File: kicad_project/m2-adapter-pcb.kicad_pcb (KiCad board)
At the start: 2 copper layers, 102 x 43 mm, 29 parts, among them J1 SATA-7P, J2 JST S2B-PH-K-S, J3 Bus_M.2_Socket_B, U1 LMR33630ADDA

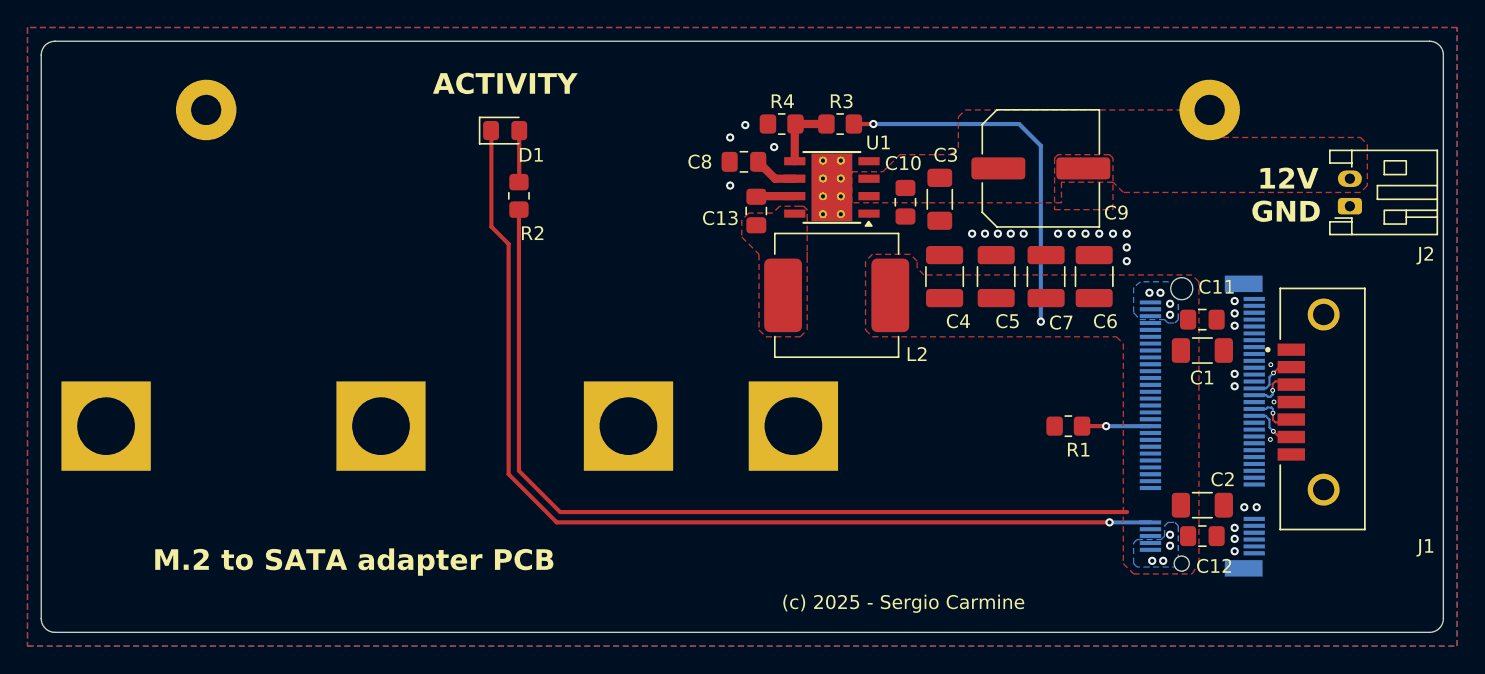
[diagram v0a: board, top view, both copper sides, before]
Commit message: Buck converter redesign
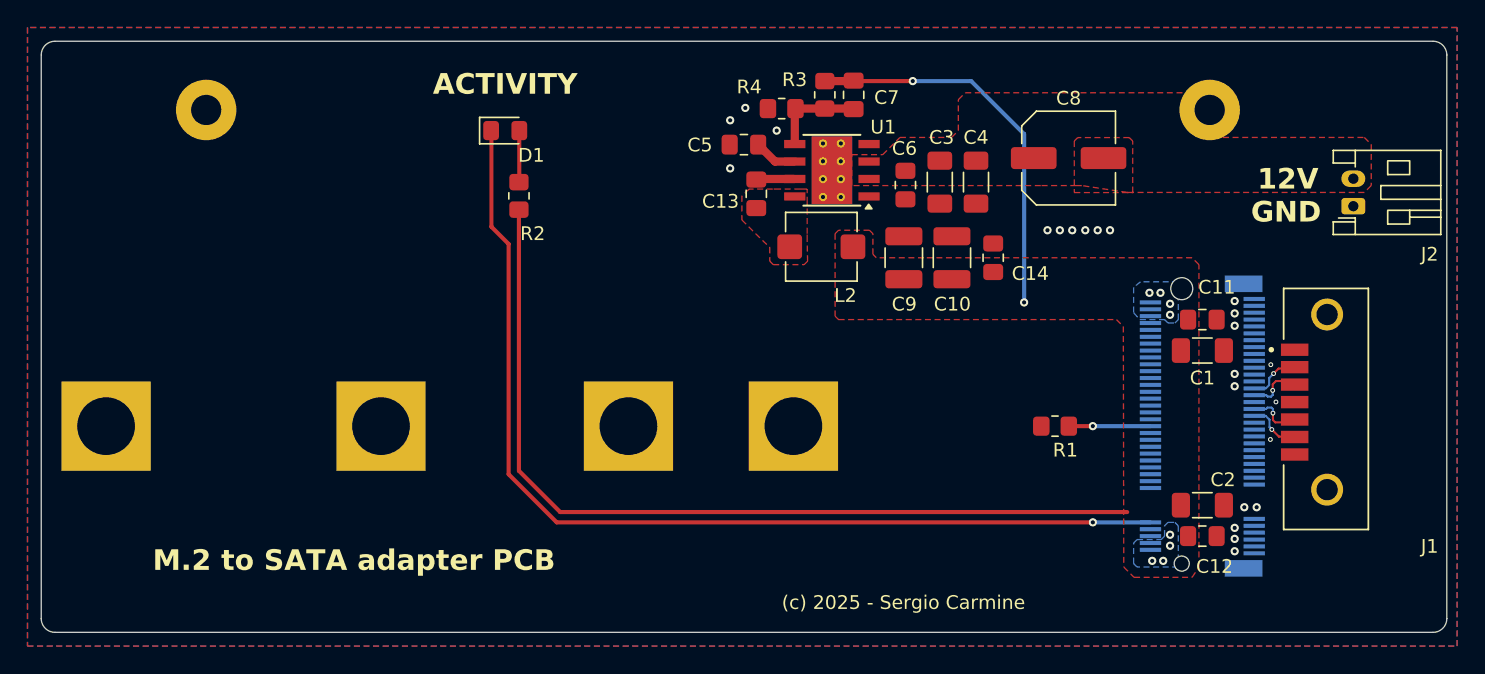
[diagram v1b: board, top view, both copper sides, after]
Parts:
- removed the C5 at (169.1, 64.1)
- removed the C6 at (172.6, 64.1)
- added C14: 0.1uF, Capacitor_SMD:C_0805_2012Metric_Pad1.18x1.45mm_HandSolder, F.Cu at (165.2, 62.8)
- added C4: 10uF, Capacitor_SMD:C_1206_3216Metric_Pad1.33x1.80mm_HandSolder, F.Cu at (164.0, 57.2)
- added C7: 4.7pF, Capacitor_SMD:C_0805_2012Metric_Pad1.18x1.45mm_HandSolder, F.Cu at (155.1, 50.9)
- C8: renamed from C9; value 100uF -> 47uF; footprint Capacitor_SMD:C_Elec_8x6.2 -> Capacitor_SMD:C_Elec_6.3x5.8
- L2: value 6.8uH -> 2.2uH; footprint m2-adapter-pcb:L_MPX1D0840 -> m2-adapter-pcb:L_AMDLA4530S
- U1: value LMR33630ADDA -> LMR33630BDDA; footprint Package_SO:Texas_HSOP-8-1EP_3.9x4.9mm_P1.27mm_ThermalVias -> m2-adapter-pcb:Texas_HSOP-8-1EP_3.9x4.9mm_P1.27mm_ThermalVias_HandSolder
- moved L2 3.71 mm to (152.8, 62.0)
- moved C10 3.50 mm to (162.2, 62.8)
- moved C9 3.27 mm to (158.8, 62.8)
- moved R3 2.40 mm to (153.0, 50.9), turned to 90 degrees
- moved C8 2.15 mm to (170.7, 55.5)
- moved C13 1.25 mm to (148.0, 58.1)
- moved C3 1.25 mm to (161.4, 57.2)
- moved C5 1.25 mm to (147.1, 54.5)
- moved C6 1.25 mm to (158.9, 57.5)
- moved U1 1.25 mm to (153.5, 56.4)
- moved R4 1.12 mm to (149.9, 51.9)
- moved R1 0.97 mm to (169.8, 75.0)
- moved J1 0.25 mm to (189.5, 73.8)
- moved J2 0.25 mm to (191.4, 59.0)
- renumbered C7 to C10, C8 to C5, C10 to C6, C4 to C9
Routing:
- net Net-(U1-FB): track 4.98 -> 7.02 mm
- net Net-(J3-DEVSLP): track 4.97 -> 5.94 mm
- net GND: vias 30 -> 23
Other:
- board size 102 x 43 mm -> 102.2 x 43 mm
